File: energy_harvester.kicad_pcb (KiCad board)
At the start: 2 copper layers, 60 x 25 mm, 13 parts, among them IC1 LTC3108EGN-1-PBF, J1 Conn_01x02_Female, J2 Conn_01x02_Female, Q1 RUM002N02T2L

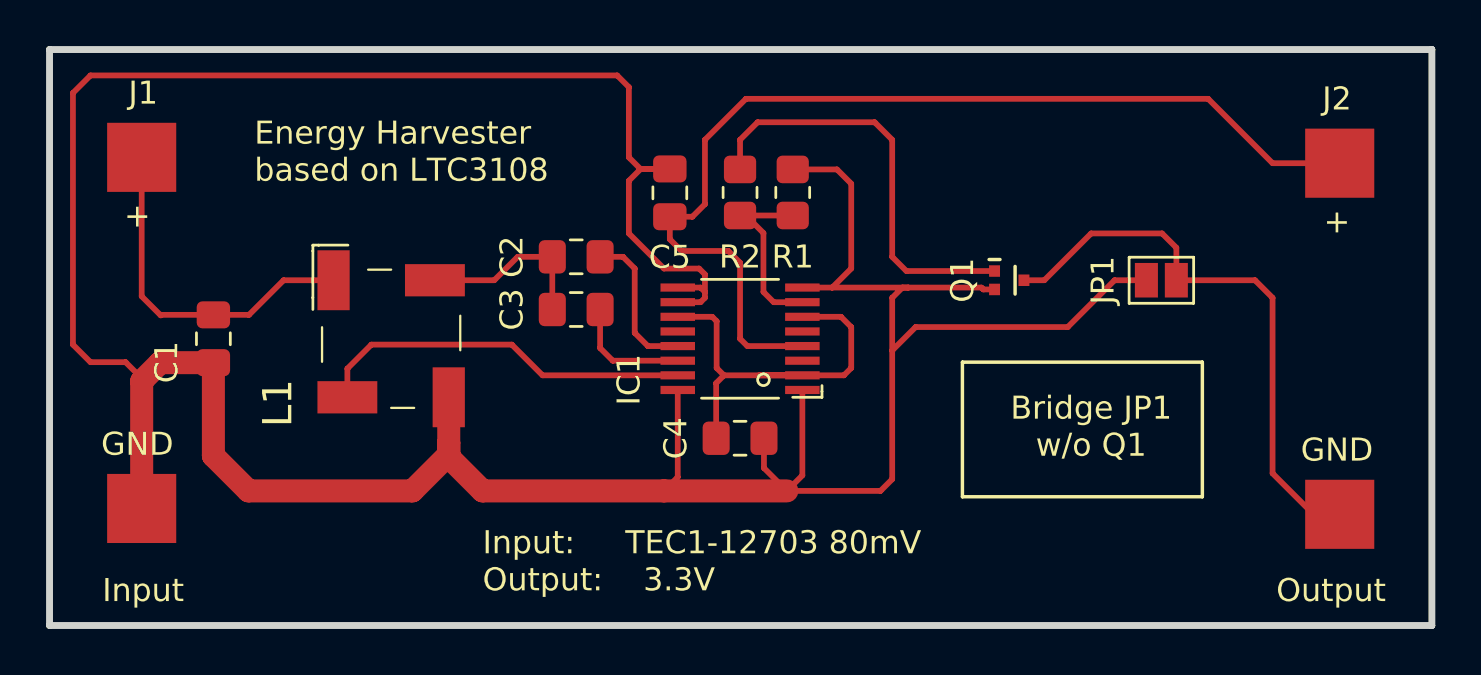
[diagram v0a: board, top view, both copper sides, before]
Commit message: Update footprints
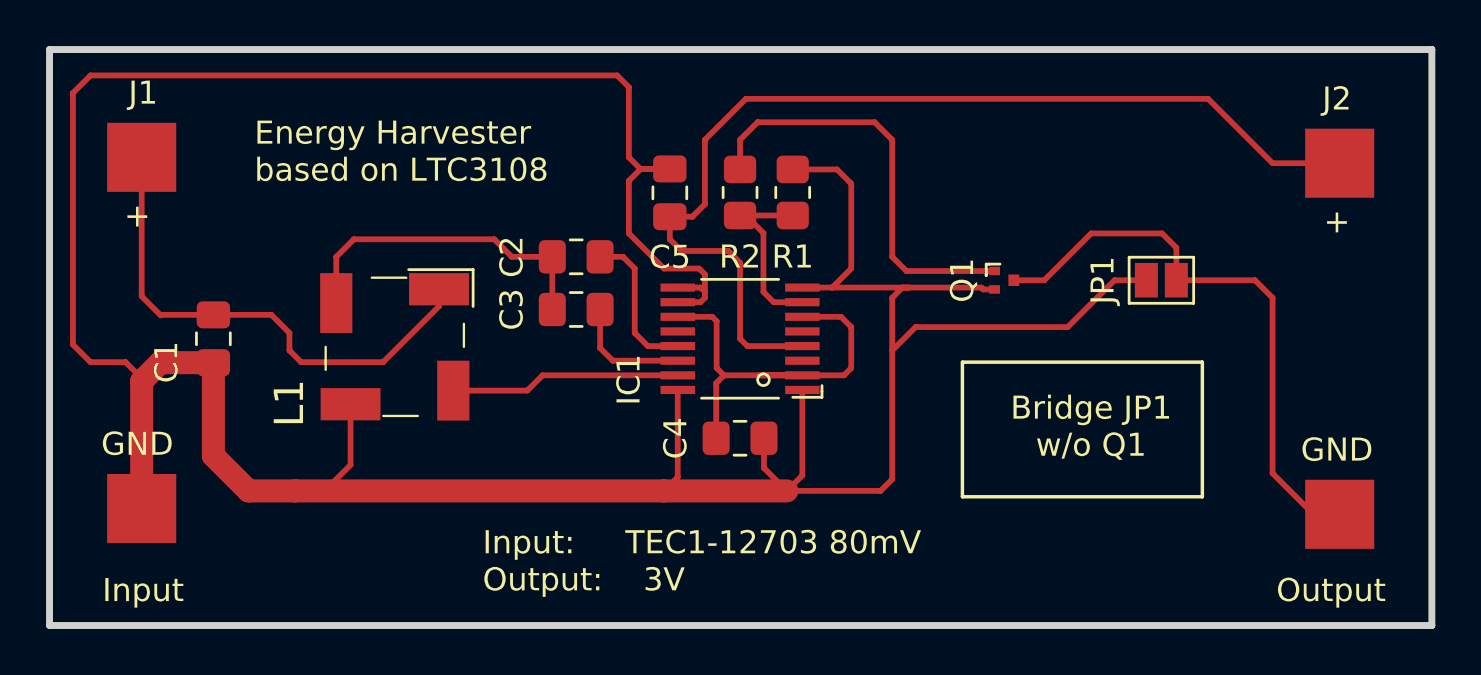
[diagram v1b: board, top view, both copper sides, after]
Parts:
- moved L1 0.51 mm to (109.0, 89.2), turned to 180 degrees
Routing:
- net Net-(C1-Pad1): track 15.3 -> 22.3 mm
- net /SW: track 16.6 -> 10.0 mm
- net Net-(C2-Pad1): track 7.80 -> 14.3 mm
- net GND: track 153.2 -> 154.3 mm
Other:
- board text added: "Input: TEC1-12703 80mV Output: 3V"
- board text removed: "Input: TEC1-12703 80mV Output: 3.3V"
